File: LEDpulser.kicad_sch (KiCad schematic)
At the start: 85 parts, among them J1 RJHSE-5380, J2 EPS.00.250.NTN, J3 EPS.00.250.NTN, J4 EB21A-04-D, J5 EPL.0S.302.HLN, Q1 DMP32D4S, Q2 DMN3028LQ-7, Q3 DMN3028LQ-7, SW1 BST11T2AVR, U1 74AHCT123APW,118, U10 LT3082EST#TRPBF, U2 74AHCT123APW,118, U3 74AHCT123APW,118, U4 SN74LVC2G74, U5 LT1117, U6 IXDI602SIATR, U7 NE555S-13, U8 PM8834, U9 PM8834

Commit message: Added pdf schematic.
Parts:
- R4: value 50 -> 0
- RV1: value 2Meg -> 100k
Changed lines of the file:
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@@
       (effects (font (size 1.27 1.27)) (justify left))
     )
-    (property "Value" "50" (id 1) (at 374.65 92.075 90))
+    (property "Value" "0" (id 1) (at 374.65 92.075 90))
     (property "Footprint" "Resistor_SMD:R_0603_1608Metric" (id 2) (at 376.428 92.075 90)
       (effects (font (size 1.27 1.27)) hide)
@@
       (effects (font (size 1.27 1.27)) (justify left))
     )
-    (property "Value" "2Meg" (id 1) (at 248.92 62.865 90))
+    (property "Value" "100k" (id 1) (at 248.92 62.865 90))
     (property "Footprint" "Potentiometer_THT:Potentiometer_Bourns_3266X_Horizontal" (id 2) (at 248.92 62.865 0)
       (effects (font (size 1.27 1.27)) hide)
@@
     )
     (path "/71b49a57-4df0-45e4-b6d3-2ded9723958b"
-      (reference "R4") (unit 1) (value "50") (footprint "Resistor_SMD:R_0603_1608Metric")
+      (reference "R4") (unit 1) (value "0") (footprint "Resistor_SMD:R_0603_1608Metric")
     )
     (path "/108ebf47-c687-4a07-92ce-253866903f37"
@@
     )
     (path "/dac9bdf9-8143-436a-9f76-17c124fa3cd8"
-      (reference "RV1") (unit 1) (value "2Meg") (footprint "Potentiometer_THT:Potentiometer_Bourns_3266X_Horizontal")
+      (reference "RV1") (unit 1) (value "100k") (footprint "Potentiometer_THT:Potentiometer_Bourns_3266X_Horizontal")
     )
     (path "/ee34309b-73a3-464c-a6d2-cc3bde3498d4"

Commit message: Fixed issue with shorts on RJ-45 connector shorting out HV regulator.
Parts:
- added R27: 10k, Resistor_SMD:R_0603_1608Metric, symbol Device:R
- U6: value IXDI602SIATR -> IXDN602SIATR
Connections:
- net CAP_VOLTAGE_OUT: now also R27.2; no longer C24.1, C26.1, D2.2 (A), R24.2, R26.2, U10.2 (VO)
- new net CAP_VOLTAGE: C24.1, C26.1, D2.2 (A), R24.2, R26.2, R27.1, U10.2 (VO)
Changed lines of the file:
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@@
     (stroke (width 0) (type default) (color 0 0 0 0))
   )
+  (wire (pts (xy 345.44 41.148) (xy 382.27 41.148))
+    (stroke (width 0) (type default) (color 0 0 0 0))
+  )
   (wire (pts (xy 23.495 92.075) (xy 23.495 94.615))
     (stroke (width 0) (type default) (color 0 0 0 0))
@@
     (stroke (width 0) (type default) (color 0 0 0 0))
   )
-  (wire (pts (xy 337.82 41.148) (xy 382.27 41.148))
-    (stroke (width 0) (type default) (color 0 0 0 0))
-  )
   (wire (pts (xy 144.145 86.36) (xy 144.145 82.55))
     (stroke (width 0) (type default) (color 0 0 0 0))
@@
     (effects (font (size 1.27 1.27)) (justify left bottom))
   )
+  (label "CAP_VOLTAGE" (at 309.372 41.148 0)
+    (effects (font (size 1.27 1.27)) (justify left bottom))
+  )
   (global_label "SU_INHIBIT" (shape input) (at 254.635 103.505 270) (fields_autoplaced)
     (effects (font (size 1.27 1.27)) (justify right))
@@
     (pin "1")
   )
+  (symbol (lib_id "Device:R") (at 341.63 41.148 90) (unit 1)
+    (in_bom yes) (on_board yes)
+    (property "Reference" "R27" (id 0) (at 341.63 39.116 90))
+    (property "Value" "10k" (id 1) (at 341.63 41.148 90))
+    (property "Footprint" "Resistor_SMD:R_0603_1608Metric" (id 2) (at 341.63 42.926 90)
+      (effects (font (size 1.27 1.27)) hide)
+    )
+    (property "Datasheet" "~" (id 3) (at 341.63 41.148 0)
+      (effects (font (size 1.27 1.27)) hide)
+    )
+    (pin "1")
+    (pin "2")
+  )
   (symbol (lib_id "power:GND") (at 168.275 34.925 0) (unit 1)
     (in_bom yes) (on_board yes) (fields_autoplaced)
@@
       (effects (font (size 1.27 1.27)) (justify left))
     )
-    (property "Value" "IXDI602SIATR" (id 1) (at 287.7694 88.3436 0)
+    (property "Value" "IXDN602SIATR" (id 1) (at 287.7694 88.3436 0)
       (effects (font (size 1.27 1.27)) (justify left))
     )
@@
       (reference "R26") (unit 1) (value "DNP") (footprint "Resistor_SMD:R_0603_1608Metric")
     )
+    (path "/755ec021-528e-4493-99b4-197d8699447f"
+      (reference "R27") (unit 1) (value "10k") (footprint "Resistor_SMD:R_0603_1608Metric")
+    )
     (path "/dac9bdf9-8143-436a-9f76-17c124fa3cd8"
       (reference "RV1") (unit 1) (value "100k") (footprint "Potentiometer_THT:Potentiometer_Bourns_3266X_Horizontal")
@@
     )
     (path "/d767f2ff-12ec-4778-96cb-3fdd7a473d60"
-      (reference "U6") (unit 1) (value "IXDI602SIATR") (footprint "Package_SO:SO-8_3.9x4.9mm_P1.27mm")
+      (reference "U6") (unit 1) (value "IXDN602SIATR") (footprint "Package_SO:SO-8_3.9x4.9mm_P1.27mm")
     )
     (path "/714276b4-c6fd-4b87-bcef-9d66d9e07653"

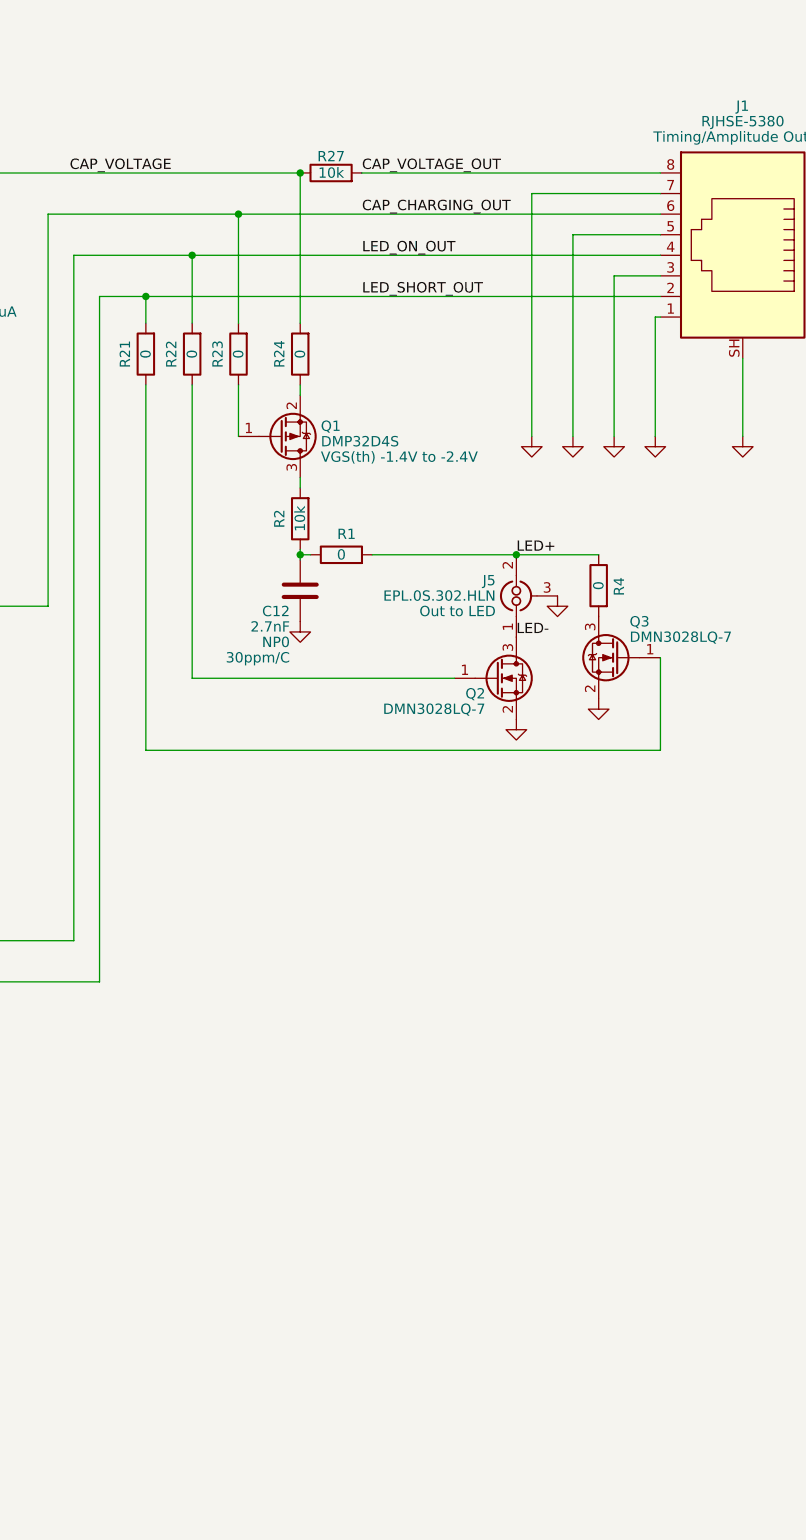
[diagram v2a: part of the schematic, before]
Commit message: Added resistors to prevent shorting power through outputs on RJ45.
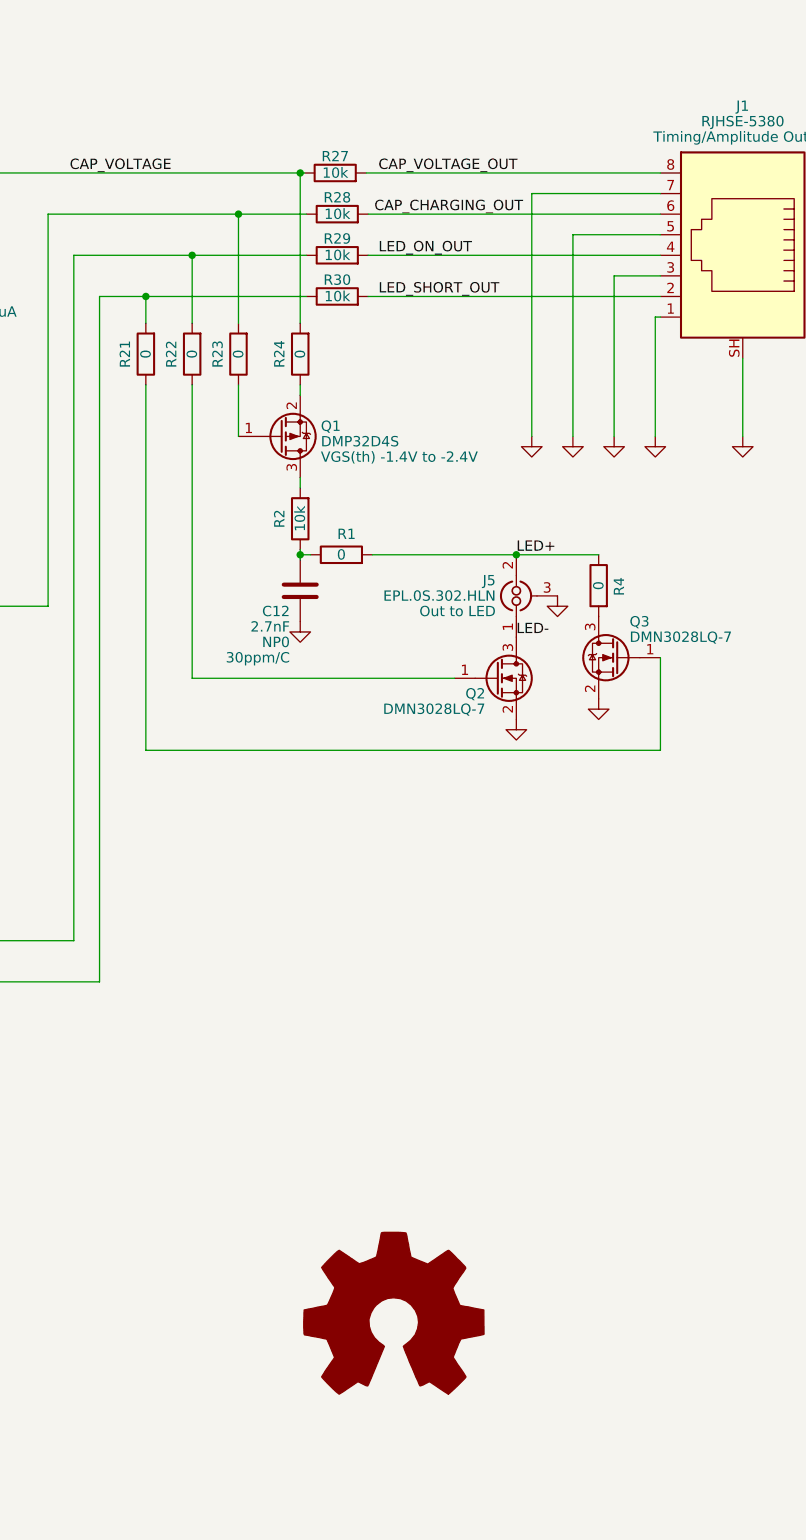
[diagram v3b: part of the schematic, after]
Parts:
- added R28, R29, R30: 10k, Resistor_SMD:R_0603_1608Metric, symbol Device:R
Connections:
- net CAP_CHARGING_OUT: now also R28.2; no longer R23.2, U6.7 (OUT_A)
- net LED_ON_OUT: now also R29.2; no longer R22.2, U8.5 (OUT_B)
- net LED_SHORT_OUT: now also R30.2; no longer R21.2, U8.7 (OUT_A)
- new net: R22.2, R29.1, U8.5 (OUT_B)
- new net: R21.2, R30.1, U8.7 (OUT_A)
- new net: R23.2, R28.1, U6.7 (OUT_A)
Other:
- moved on the sheet: R27
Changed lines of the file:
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@@
   (junction (at 285.75 41.148) (diameter 0) (color 0 0 0 0)
   )
-  (junction (at 337.82 41.148) (diameter 0) (color 0 0 0 0)
-  )
   (junction (at 188.595 82.55) (diameter 0) (color 0 0 0 0)
   )
@@
   (junction (at 109.22 39.37) (diameter 0) (color 0 0 0 0)
   )
+  (junction (at 337.82 41.148) (diameter 0) (color 0 0 0 0)
+  )
   (junction (at 285.75 74.295) (diameter 0) (color 0 0 0 0)
   )
@@
     (stroke (width 0) (type default) (color 0 0 0 0))
   )
+  (wire (pts (xy 345.948 41.148) (xy 382.27 41.148))
+    (stroke (width 0) (type default) (color 0 0 0 0))
+  )
   (wire (pts (xy 176.53 27.305) (xy 176.53 27.94))
     (stroke (width 0) (type default) (color 0 0 0 0))
@@
     (stroke (width 0) (type default) (color 0 0 0 0))
   )
+  (wire (pts (xy 337.82 41.148) (xy 338.328 41.148))
+    (stroke (width 0) (type default) (color 0 0 0 0))
+  )
   (wire (pts (xy 324.485 67.31) (xy 324.485 103.505))
     (stroke (width 0) (type default) (color 0 0 0 0))
@@
     (stroke (width 0) (type default) (color 0 0 0 0))
   )
-  (wire (pts (xy 345.44 41.148) (xy 382.27 41.148))
-    (stroke (width 0) (type default) (color 0 0 0 0))
-  )
   (wire (pts (xy 23.495 92.075) (xy 23.495 94.615))
     (stroke (width 0) (type default) (color 0 0 0 0))
@@
     (stroke (width 0) (type default) (color 0 0 0 0))
   )
-  (wire (pts (xy 318.77 56.388) (xy 382.27 56.388))
+  (wire (pts (xy 318.77 56.388) (xy 338.582 56.388))
     (stroke (width 0) (type default) (color 0 0 0 0))
   )
@@
     (stroke (width 0) (type default) (color 0 0 0 0))
   )
-  (wire (pts (xy 330.2 46.228) (xy 382.27 46.228))
+  (wire (pts (xy 330.2 46.228) (xy 338.582 46.228))
     (stroke (width 0) (type default) (color 0 0 0 0))
   )
@@
     (stroke (width 0) (type default) (color 0 0 0 0))
   )
+  (wire (pts (xy 346.202 46.228) (xy 382.27 46.228))
+    (stroke (width 0) (type default) (color 0 0 0 0))
+  )
   (wire (pts (xy 154.305 135.89) (xy 154.94 135.89))
     (stroke (width 0) (type default) (color 0 0 0 0))
@@
     (stroke (width 0) (type default) (color 0 0 0 0))
   )
-  (wire (pts (xy 324.485 51.308) (xy 382.27 51.308))
+  (wire (pts (xy 324.485 51.308) (xy 338.582 51.308))
     (stroke (width 0) (type default) (color 0 0 0 0))
   )
@@
     (stroke (width 0) (type default) (color 0 0 0 0))
   )
+  (wire (pts (xy 346.202 56.388) (xy 382.27 56.388))
+    (stroke (width 0) (type default) (color 0 0 0 0))
+  )
   (wire (pts (xy 381.635 58.928) (xy 381.635 73.66))
     (stroke (width 0) (type default) (color 0 0 0 0))
@@
     (stroke (width 0) (type default) (color 0 0 0 0))
   )
+  (wire (pts (xy 346.202 51.308) (xy 382.27 51.308))
+    (stroke (width 0) (type default) (color 0 0 0 0))
+  )
   (wire (pts (xy 188.595 139.7) (xy 192.405 139.7))
     (stroke (width 0) (type default) (color 0 0 0 0))
@@
     (effects (font (size 1.27 1.27)) (justify left bottom))
   )
-  (label "CAP_VOLTAGE_OUT" (at 345.44 41.148 0)
+  (label "CAP_VOLTAGE_OUT" (at 347.472 41.148 0)
     (effects (font (size 1.27 1.27)) (justify left bottom))
   )
@@
     (effects (font (size 1.27 1.27)) (justify left bottom))
   )
-  (label "CAP_CHARGING_OUT" (at 345.44 46.228 0)
+  (label "CAP_CHARGING_OUT" (at 346.964 46.228 0)
     (effects (font (size 1.27 1.27)) (justify left bottom))
   )
-  (label "LED_SHORT_OUT" (at 345.44 56.388 0)
+  (label "LED_SHORT_OUT" (at 347.472 56.388 0)
     (effects (font (size 1.27 1.27)) (justify left bottom))
   )
@@
     (effects (font (size 1.27 1.27)) (justify left bottom))
   )
-  (label "LED_ON_OUT" (at 345.44 51.308 0)
+  (label "LED_ON_OUT" (at 347.472 51.308 0)
     (effects (font (size 1.27 1.27)) (justify left bottom))
   )
@@
     (pin "3")
   )
+  (symbol (lib_id "Graphic:Logo_Open_Hardware_Large") (at 349.377 183.134 0) (unit 1)
+    (in_bom yes) (on_board yes) (fields_autoplaced)
+    (property "Reference" "#LOGO1" (id 0) (at 349.377 170.434 0)
+      (effects (font (size 1.27 1.27)) hide)
+    )
+    (property "Value" "Logo_Open_Hardware_Large" (id 1) (at 349.377 193.294 0)
+      (effects (font (size 1.27 1.27)) hide)
+    )
+    (property "Footprint" "" (id 2) (at 349.377 183.134 0)
+      (effects (font (size 1.27 1.27)) hide)
+    )
+    (property "Datasheet" "~" (id 3) (at 349.377 183.134 0)
+      (effects (font (size 1.27 1.27)) hide)
+    )
+  )
   (symbol (lib_id "power:GND") (at 67.945 198.12 90) (mirror x) (unit 1)
     (in_bom yes) (on_board yes) (fields_autoplaced)
@@
     (pin "2")
   )
+  (symbol (lib_id "Device:R") (at 342.392 46.228 90) (unit 1)
+    (in_bom yes) (on_board yes)
+    (property "Reference" "R28" (id 0) (at 342.392 44.196 90))
+    (property "Value" "10k" (id 1) (at 342.392 46.228 90))
+    (property "Footprint" "Resistor_SMD:R_0603_1608Metric" (id 2) (at 342.392 48.006 90)
+      (effects (font (size 1.27 1.27)) hide)
+    )
+    (property "Datasheet" "~" (id 3) (at 342.392 46.228 0)
+      (effects (font (size 1.27 1.27)) hide)
+    )
+    (pin "1")
+    (pin "2")
+  )
   (symbol (lib_id "Connector:Conn_01x04_Female") (at 25.4 68.58 180) (unit 1)
     (in_bom yes) (on_board yes) (fields_autoplaced)
@@
     (pin "1")
   )
-  (symbol (lib_id "Device:R") (at 341.63 41.148 90) (unit 1)
+  (symbol (lib_id "Device:R") (at 342.138 41.148 90) (unit 1)
     (in_bom yes) (on_board yes)
-    (property "Reference" "R27" (id 0) (at 341.63 39.116 90))
-    (property "Value" "10k" (id 1) (at 341.63 41.148 90))
-    (property "Footprint" "Resistor_SMD:R_0603_1608Metric" (id 2) (at 341.63 42.926 90)
+    (property "Reference" "R27" (id 0) (at 342.138 39.116 90))
+    (property "Value" "10k" (id 1) (at 342.138 41.148 90))
+    (property "Footprint" "Resistor_SMD:R_0603_1608Metric" (id 2) (at 342.138 42.926 90)
       (effects (font (size 1.27 1.27)) hide)
     )
-    (property "Datasheet" "~" (id 3) (at 341.63 41.148 0)
+    (property "Datasheet" "~" (id 3) (at 342.138 41.148 0)
       (effects (font (size 1.27 1.27)) hide)
     )
@@
     )
   )
+  (symbol (lib_id "Device:R") (at 342.392 51.308 90) (unit 1)
+    (in_bom yes) (on_board yes)
+    (property "Reference" "R29" (id 0) (at 342.392 49.276 90))
+    (property "Value" "10k" (id 1) (at 342.392 51.308 90))
+    (property "Footprint" "Resistor_SMD:R_0603_1608Metric" (id 2) (at 342.392 53.086 90)
+      (effects (font (size 1.27 1.27)) hide)
+    )
+    (property "Datasheet" "~" (id 3) (at 342.392 51.308 0)
+      (effects (font (size 1.27 1.27)) hide)
+    )
+    (pin "1")
+    (pin "2")
+  )
   (symbol (lib_id "power:VCC") (at 38.1 92.075 0) (unit 1)
     (in_bom yes) (on_board yes)
@@
     (pin "1")
   )
+  (symbol (lib_id "Device:R") (at 342.392 56.388 90) (unit 1)
+    (in_bom yes) (on_board yes)
+    (property "Reference" "R30" (id 0) (at 342.392 54.356 90))
+    (property "Value" "10k" (id 1) (at 342.392 56.388 90))
+    (property "Footprint" "Resistor_SMD:R_0603_1608Metric" (id 2) (at 342.392 58.166 90)
+      (effects (font (size 1.27 1.27)) hide)
+    )
+    (property "Datasheet" "~" (id 3) (at 342.392 56.388 0)
+      (effects (font (size 1.27 1.27)) hide)
+    )
+    (pin "1")
+    (pin "2")
+  )
   (symbol (lib_id "Device:C") (at 104.775 96.52 0) (unit 1)
     (in_bom yes) (on_board yes)
@@
   )
   (symbol_instances
+    (path "/2da0ab7d-f0ca-4fa2-9084-e8291cef8796"
+      (reference "#LOGO1") (unit 1) (value "Logo_Open_Hardware_Large") (footprint "")
+    )
     (path "/02bc5d26-72d4-4065-b41e-b9f1fb0cc22c"
       (reference "#PWR01") (unit 1) (value "VCC") (footprint "")
@@
       (reference "R27") (unit 1) (value "10k") (footprint "Resistor_SMD:R_0603_1608Metric")
     )
+    (path "/59d13ece-c564-4c59-bfd9-780db895bcc2"
+      (reference "R28") (unit 1) (value "10k") (footprint "Resistor_SMD:R_0603_1608Metric")
+    )
+    (path "/7da05323-2977-4b81-8678-b919e91d668e"
+      (reference "R29") (unit 1) (value "10k") (footprint "Resistor_SMD:R_0603_1608Metric")
+    )
+    (path "/dc0607e4-1af3-4525-9e3e-37bb525b9e45"
+      (reference "R30") (unit 1) (value "10k") (footprint "Resistor_SMD:R_0603_1608Metric")
+    )
     (path "/dac9bdf9-8143-436a-9f76-17c124fa3cd8"
